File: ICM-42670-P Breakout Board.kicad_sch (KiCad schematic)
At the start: 12 parts, among them J2 Conn_01x09_Pin, U1 ICM-42670-P, U2 MCP1700x-330xxTT

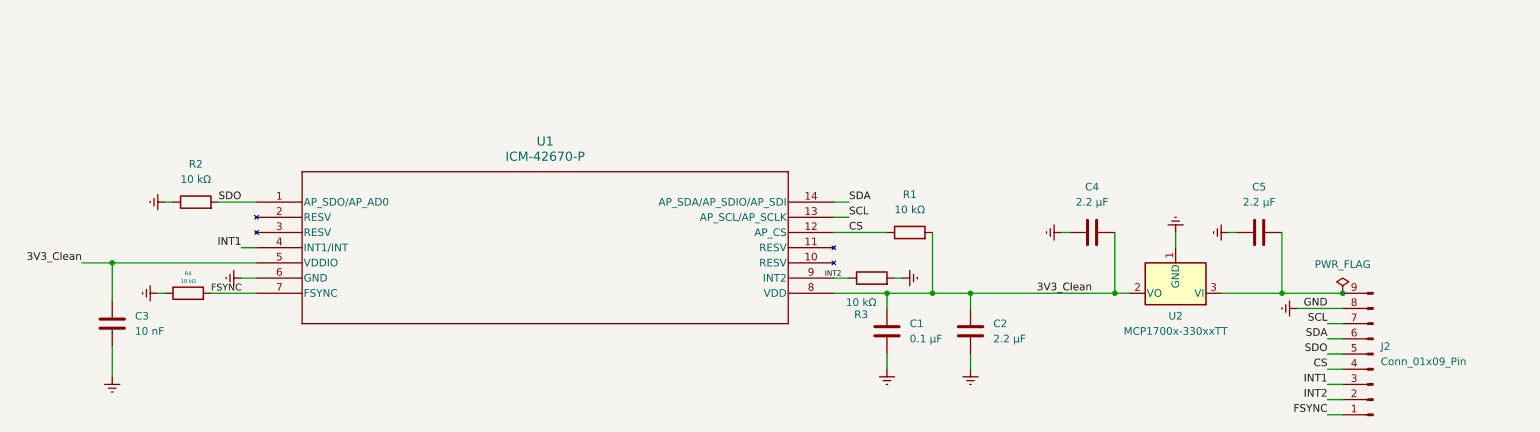
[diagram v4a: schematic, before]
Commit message: Got rid of Resistor on SDO
SDO resister can interfere with SPI and i3C comms, better to let MCU or user Control it
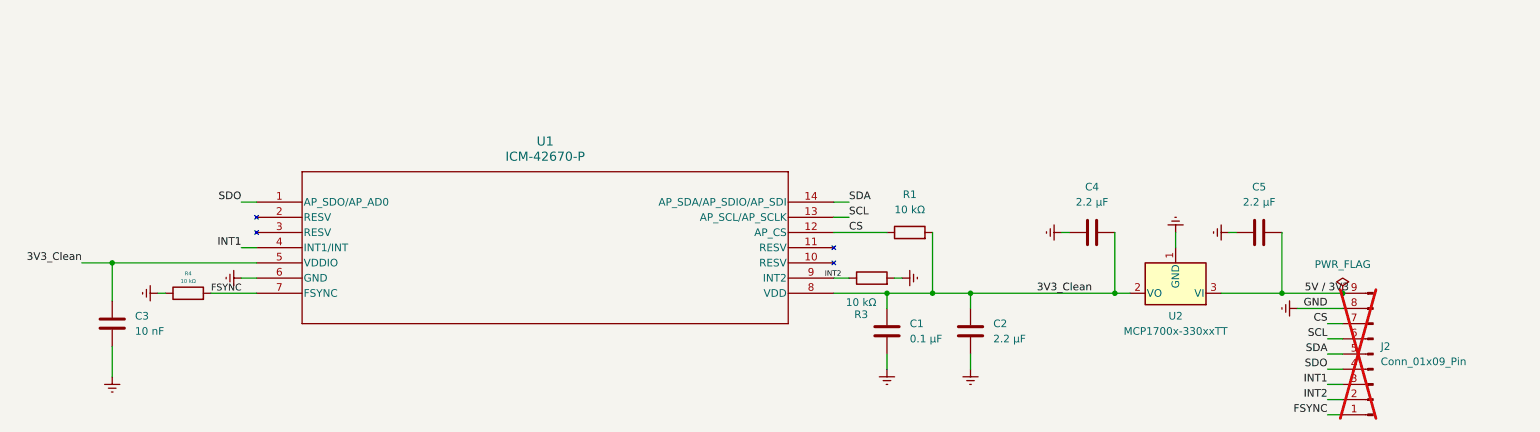
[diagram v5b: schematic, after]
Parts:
- removed R2: 10 kΩ, Resistor_SMD:R_0402_1005Metric, symbol Device:R
- J2: now not fitted
- R1, R3, R4: Specification (none) -> ±1% 0.0625 W (1/16 W)
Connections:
- net CS: now also J2.7 (Pin_7); no longer J2.4 (Pin_4)
- net SCL: now also J2.6 (Pin_6); no longer J2.7 (Pin_7)
- net SDA: now also J2.5 (Pin_5); no longer J2.6 (Pin_6)
- net SDO: now also J2.4 (Pin_4); no longer J2.5 (Pin_5)
- net 5V / 3V3: now reaches C5.2, J2.9 (Pin_9), U2.3 (VI)
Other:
- company: (none) -> Anthony Hua / SleepPandas
- title: (none) -> ICM-42670-P Motion Sensor Breakout with Power Regulation
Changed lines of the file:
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@@
 	(generator_version "9.0")
 	(paper "A4")
+	(title_block
+		(title "ICM-42670-P Motion Sensor Breakout with Power Regulation")
+		(date "2026-MARCH-07")
+		(rev "v1.0")
+		(company "Anthony Hua / SleepPandas")
+	)
 	(junction
 		(at 241.3 101.6)
@@
 	(wire
 		(pts
-			(xy 238.76 111.76) (xy 241.3 111.76)
+			(xy 238.76 106.68) (xy 241.3 106.68)
 		)
 		(stroke
@@
 	(wire
 		(pts
-			(xy 238.76 109.22) (xy 241.3 109.22)
+			(xy 156.21 86.36) (xy 158.75 86.36)
 		)
 		(stroke
@@
 	(wire
 		(pts
-			(xy 156.21 86.36) (xy 158.75 86.36)
+			(xy 57.15 86.36) (xy 59.69 86.36)
 		)
 		(stroke
@@
 	(wire
 		(pts
-			(xy 231.14 101.6) (xy 241.3 101.6)
-		)
-		(stroke
-			(width 0)
-			(type default)
-		)
-	)
-	(wire
-		(pts
-			(xy 238.76 114.3) (xy 241.3 114.3)
+			(xy 233.68 104.14) (xy 241.3 104.14)
 		)
 		(stroke
@@
 	(wire
 		(pts
-			(xy 233.68 104.14) (xy 241.3 104.14)
+			(xy 220.98 101.6) (xy 231.14 101.6)
 		)
 		(stroke
@@
 	(wire
 		(pts
-			(xy 238.76 106.68) (xy 241.3 106.68)
+			(xy 238.76 121.92) (xy 241.3 121.92)
 		)
 		(stroke
@@
 	(wire
 		(pts
-			(xy 220.98 101.6) (xy 231.14 101.6)
+			(xy 222.25 91.44) (xy 223.52 91.44)
 		)
 		(stroke
@@
 	(wire
 		(pts
-			(xy 238.76 121.92) (xy 241.3 121.92)
+			(xy 238.76 119.38) (xy 241.3 119.38)
 		)
 		(stroke
@@
 	(wire
 		(pts
-			(xy 222.25 91.44) (xy 223.52 91.44)
+			(xy 57.15 93.98) (xy 59.69 93.98)
 		)
 		(stroke
@@
 	(wire
 		(pts
-			(xy 238.76 119.38) (xy 241.3 119.38)
+			(xy 238.76 116.84) (xy 241.3 116.84)
 		)
 		(stroke
@@
 	(wire
 		(pts
-			(xy 57.15 93.98) (xy 59.69 93.98)
+			(xy 231.14 91.44) (xy 231.14 101.6)
 		)
 		(stroke
@@
 	(wire
 		(pts
-			(xy 238.76 116.84) (xy 241.3 116.84)
+			(xy 179.07 101.6) (xy 203.2 101.6)
 		)
 		(stroke
@@
 	(wire
 		(pts
-			(xy 231.14 91.44) (xy 231.14 101.6)
+			(xy 35.56 110.49) (xy 35.56 115.57)
 		)
 		(stroke
@@
 	(wire
 		(pts
-			(xy 179.07 101.6) (xy 203.2 101.6)
+			(xy 238.76 109.22) (xy 241.3 109.22)
 		)
 		(stroke
@@
 	(wire
 		(pts
-			(xy 35.56 110.49) (xy 35.56 115.57)
+			(xy 231.14 101.6) (xy 241.3 101.6)
 		)
 		(stroke
@@
 	(wire
 		(pts
-			(xy 53.34 86.36) (xy 59.69 86.36)
+			(xy 165.1 111.76) (xy 165.1 114.3)
 		)
 		(stroke
@@
 	(wire
 		(pts
-			(xy 165.1 111.76) (xy 165.1 114.3)
+			(xy 166.37 99.06) (xy 167.64 99.06)
 		)
 		(stroke
@@
 	(wire
 		(pts
-			(xy 44.45 86.36) (xy 45.72 86.36)
+			(xy 238.76 111.76) (xy 241.3 111.76)
 		)
 		(stroke
@@
 	(wire
 		(pts
-			(xy 166.37 99.06) (xy 167.64 99.06)
+			(xy 172.72 101.6) (xy 179.07 101.6)
 		)
 		(stroke
@@
 	(wire
 		(pts
-			(xy 172.72 101.6) (xy 179.07 101.6)
+			(xy 165.1 101.6) (xy 165.1 104.14)
 		)
 		(stroke
@@
 	(wire
 		(pts
-			(xy 165.1 101.6) (xy 165.1 104.14)
+			(xy 238.76 114.3) (xy 241.3 114.3)
 		)
 		(stroke
@@
 	)
 	(label "CS"
-		(at 238.76 114.3 180)
+		(at 238.76 106.68 180)
 		(effects
 			(font
@@
 		)
 	)
+	(label "5V {slash} 3V3"
+		(at 234.95 101.6 0)
+		(effects
+			(font
+				(size 1.27 1.27)
+			)
+			(justify left bottom)
+		)
+	)
 	(label "SCL"
 		(at 158.75 88.9 0)
@@
 	)
 	(label "SDO"
-		(at 238.76 111.76 180)
+		(at 238.76 114.3 180)
 		(effects
 			(font
@@
 	)
 	(label "SDA"
-		(at 238.76 109.22 180)
+		(at 238.76 111.76 180)
 		(effects
 			(font
@@
 	)
 	(label "SCL"
-		(at 238.76 106.68 180)
+		(at 238.76 109.22 180)
 		(effects
 			(font
@@
 		(in_bom yes)
 		(on_board yes)
-		(dnp no)
+		(dnp yes)
 		(fields_autoplaced yes)
 		(property "Reference" "J2"
@@
 			)
 		)
+		(property "Specification" "±1% 0.0625 W (1/16 W)"
+			(at 168.91 91.44 90)
+			(effects
+				(font
+					(size 1.27 1.27)
+				)
+				(hide yes)
+			)
+		)
 		(pin "2"
 		)
@@
 	(symbol
 		(lib_id "power:Earth")
-		(at 44.45 86.36 270)
-		(unit 1)
-		(exclude_from_sim no)
-		(in_bom yes)
-		(on_board yes)
-		(dnp no)
-		(fields_autoplaced yes)
-		(property "Reference" "#PWR017"
-			(at 38.1 86.36 0)
-			(effects
-				(font
-					(size 1.27 1.27)
-				)
-				(hide yes)
-			)
-		)
-		(property "Value" "GND"
-			(at 40.64 86.3599 90)
-			(effects
-				(font
-					(size 1.27 1.27)
-				)
-				(justify right)
-				(hide yes)
-			)
-		)
-		(property "Footprint" ""
-			(at 44.45 86.36 0)
-			(effects
-				(font
-					(size 1.27 1.27)
-				)
-				(hide yes)
-			)
-		)
-		(property "Datasheet" "~"
-			(at 44.45 86.36 0)
-			(effects
-				(font
-					(size 1.27 1.27)
-				)
-				(hide yes)
-			)
-		)
-		(property "Description" "Power symbol creates a global label with name \"Earth\""
-			(at 44.45 86.36 0)
-			(effects
-				(font
-					(size 1.27 1.27)
-				)
-				(hide yes)
-			)
-		)
-		(pin "1"
-		)
-		(instances
-			(project ""
-				(path "/46f757aa-f0ff-4bf0-8e74-16936fa9d7c2"
-					(reference "#PWR017")
-					(unit 1)
-				)
-			)
-		)
-	)
-	(symbol
-		(lib_id "power:Earth")
 		(at 233.68 104.14 270)
 		(unit 1)
@@
 			)
 		)
+		(property "Specification" "±1% 0.0625 W (1/16 W)"
+			(at 48.26 101.6 90)
+			(effects
+				(font
+					(size 1.27 1.27)
+				)
+				(hide yes)
+			)
+		)
 		(pin "2"
 		)
@@
 	)
 	(symbol
+		(lib_name "C_1")
 		(lib_id "Device:C")
 		(at 227.33 91.44 90)
@@
 			)
 		)
+		(property "Specification" "±1% 0.0625 W (1/16 W)"
+			(at 162.56 99.06 90)
+			(effects
+				(font
+					(size 1.27 1.27)
+				)
+				(hide yes)
+			)
+		)
 		(pin "2"
 		)
@@
 	)
 	(symbol
-		(lib_id "Device:R")
-		(at 49.53 86.36 90)
-		(unit 1)
-		(exclude_from_sim no)
-		(in_bom yes)
-		(on_board yes)
-		(dnp no)
-		(fields_autoplaced yes)
-		(property "Reference" "R2"
-			(at 49.53 80.01 90)
-			(effects
-				(font
-					(size 1.27 1.27)
-				)
-			)
-		)
-		(property "Value" "10 kΩ"
-			(at 49.53 82.55 90)
-			(effects
-				(font
-					(size 1.27 1.27)
-				)
-			)
-		)
-		(property "Footprint" "Resistor_SMD:R_0402_1005Metric"
-			(at 49.53 88.138 90)
-			(effects
-				(font
-					(size 1.27 1.27)
-				)
-				(hide yes)
-			)
-		)
-		(property "Datasheet" "~"
-			(at 49.53 86.36 0)
-			(effects
-				(font
-					(size 1.27 1.27)
-				)
-				(hide yes)
-			)
-		)
-		(property "Description" "Resistor"
-			(at 49.53 86.36 0)
-			(effects
-				(font
-					(size 1.27 1.27)
-				)
-				(hide yes)
-			)
-		)
-		(pin "2"
-		)
-		(pin "1"
-		)
-		(instances
-			(project "ICM-42688-P Breakout Board"
-				(path "/46f757aa-f0ff-4bf0-8e74-16936fa9d7c2"
-					(reference "R2")
-					(unit 1)
-				)
-			)
-		)
-	)
-	(symbol
 		(lib_id "Device:C")
 		(at 179.07 107.95 0)
@@
 	)
 	(embedded_fonts no)
+	(embedded_files
+		(file
+			(name "Draw.kicad_wks")
+			(type worksheet)
+			(data |KLUv/WAECj0VAFbeXyDwWDfQsSwzzQ+NxFWaF2Yhlyyb60htn+WZmgWewXn7VFYATwBaAJ9nEf9j
+				b8QP+tgsZ1/7yZ3YeY+Hhjov2aAHrcmvDQ31mu0pO/qTfwEACAhG0vtIXgyrY1nQO+FodcbfZb/+
+				MSzmnBiVtC+2o+ylAiAgGIlMHbD7rKgQnufJiRUAf7FndqU9wqM1rf6Tv/dVYpW2rKhT/q79zkfP
+				2W/G34ctW1qiD4dee/j220Hf4CXh3LXVf10U8UebNngdgbWcsz93P7KsdrG7H9+JGXs6+9hdMNol
+				u3jKZsAQe42g20bDlByzWFgtmReiGXJWLFsGo206j8yxSVSEetWWczKuRCsWK43LHh1Nk8lsKkI3
+				/LtHzhmV/a9/jfLYH5FClfbMULS2DAGBgSZoZWAUQ1AGNhNUYnRyFY2Cut0oYgeiXlRKeSlo14uh
+				4FSyC8XiUES47MJpWiSzWGAXgpJVtMkGsZDPht3bVlxyahNu48K3HJ10grbfHZQZHFYDcLM6gIKg
+				8USGmJkSUZgkKXSARKTmqBvcLGt61Ov0GmMtRspN6ePryEhYdd4Zdt3vqhHCMWA+Vx2YBFRFjQ10
+				v7/yB/HrlrTSW8DzSTIPOJrFk+BJ19kyUKQVZo7tyclTk53NC8lJt2Oa4/JPE/OpDO4plFCTWdpW
+				DPc5ILzpriyJD7CvDGfUQECbOeXLBMFKWFQQYILlaTRUu5RqmCwbpw7iC/qfTIxJCzlohs/TEzUM
+				aMjpH31l2dzksKfcoq659NJWGwqEdOe0JwoUvHEWH/zmmPdoK2BncUu03EXv/TJsXoNLryAQxOrJ
+				KQFNTR5hDBDkWYfoUzII9kKCyauBA0PHrh4tc7bkSULLcrK2IcRN/Ia9S68mNU3TxvpvLA9Rd5nr
+				QzoGqwo=|
+			)
+			(checksum "EA453518717EB0DF5586ED4C77A0ADB3")
+		)
+	)
 )

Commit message: Got rid of Pull down Resistor for INT2
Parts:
- removed R3: 10 kΩ, Resistor_SMD:R_0402_1005Metric, symbol Device:R
- renumbered R4 to R3
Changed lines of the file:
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@@
 	)
 	(junction
+		(at 53.34 101.6)
+		(diameter 0)
+		(color 0 0 0 0)
+	)
+	(junction
 		(at 231.14 101.6)
 		(diameter 0)
@@
 	(wire
 		(pts
-			(xy 52.07 101.6) (xy 59.69 101.6)
+			(xy 53.34 106.68) (xy 53.34 101.6)
 		)
 		(stroke
@@
 	(wire
 		(pts
-			(xy 166.37 99.06) (xy 167.64 99.06)
+			(xy 238.76 111.76) (xy 241.3 111.76)
 		)
 		(stroke
@@
 	(wire
 		(pts
-			(xy 238.76 111.76) (xy 241.3 111.76)
+			(xy 172.72 101.6) (xy 179.07 101.6)
 		)
 		(stroke
@@
 	(wire
 		(pts
-			(xy 172.72 101.6) (xy 179.07 101.6)
+			(xy 165.1 101.6) (xy 165.1 104.14)
 		)
 		(stroke
@@
 	(wire
 		(pts
-			(xy 165.1 101.6) (xy 165.1 104.14)
+			(xy 238.76 114.3) (xy 241.3 114.3)
 		)
 		(stroke
@@
 	(wire
 		(pts
-			(xy 238.76 114.3) (xy 241.3 114.3)
+			(xy 35.56 96.52) (xy 59.69 96.52)
 		)
 		(stroke
@@
 	(wire
 		(pts
-			(xy 35.56 96.52) (xy 59.69 96.52)
+			(xy 53.34 101.6) (xy 52.07 101.6)
+		)
+		(stroke
+			(width 0)
+			(type default)
+		)
+	)
+	(wire
+		(pts
+			(xy 53.34 101.6) (xy 59.69 101.6)
 		)
 		(stroke
@@
 	)
 	(label "FSYNC"
-		(at 52.07 101.6 0)
+		(at 53.34 106.68 0)
 		(effects
 			(font
@@
 	(symbol
 		(lib_id "power:Earth")
-		(at 167.64 99.06 90)
-		(unit 1)
-		(exclude_from_sim no)
-		(in_bom yes)
-		(on_board yes)
-		(dnp no)
-		(fields_autoplaced yes)
-		(property "Reference" "#PWR014"
-			(at 173.99 99.06 0)
-			(effects
-				(font
-					(size 1.27 1.27)
-				)
-				(hide yes)
-			)
-		)
-		(property "Value" "GND"
-			(at 171.45 99.0599 90)
-			(effects
-				(font
-					(size 1.27 1.27)
-				)
-				(justify right)
-				(hide yes)
-			)
-		)
-		(property "Footprint" ""
-			(at 167.64 99.06 0)
-			(effects
-				(font
-					(size 1.27 1.27)
-				)
-				(hide yes)
-			)
-		)
-		(property "Datasheet" "~"
-			(at 167.64 99.06 0)
-			(effects
-				(font
-					(size 1.27 1.27)
-				)
-				(hide yes)
-			)
-		)
-		(property "Description" "Power symbol creates a global label with name \"Earth\""
-			(at 167.64 99.06 0)
-			(effects
-				(font
-					(size 1.27 1.27)
-				)
-				(hide yes)
-			)
-		)
-		(pin "1"
-		)
-		(instances
-			(project ""
-				(path "/46f757aa-f0ff-4bf0-8e74-16936fa9d7c2"
-					(reference "#PWR014")
-					(unit 1)
-				)
-			)
-		)
-	)
-	(symbol
-		(lib_id "power:Earth")
 		(at 35.56 115.57 0)
 		(unit 1)
@@
 		(on_board yes)
 		(dnp no)
-		(property "Reference" "R4"
+		(property "Reference" "R3"
 			(at 48.26 98.298 90)
 			(effects
@@
 			(project "ICM-42670-P Breakout Board"
 				(path "/46f757aa-f0ff-4bf0-8e74-16936fa9d7c2"
-					(reference "R4")
+					(reference "R3")
 					(unit 1)
 				)
@@
 					(unit 1)
 				)
-			)
-		)
-	)
-	(symbol
-		(lib_id "Device:R")
-		(at 162.56 99.06 90)
-		(unit 1)
-		(exclude_from_sim no)
-		(in_bom yes)
-		(on_board yes)
-		(dnp no)
-		(property "Reference" "R3"
-			(at 160.782 105.156 90)
-			(effects
-				(font
-					(size 1.27 1.27)
-				)
-			)
-		)
-		(property "Value" "10 kΩ"
-			(at 160.782 103.124 90)
-			(effects
-				(font
-					(size 1.27 1.27)
-				)
-			)
-		)
-		(property "Footprint" "Resistor_SMD:R_0402_1005Metric"
-			(at 162.56 100.838 90)
-			(effects
-				(font
-					(size 1.27 1.27)
-				)
-				(hide yes)
-			)
-		)
-		(property "Datasheet" "~"
-			(at 162.56 99.06 0)
-			(effects
-				(font
-					(size 1.27 1.27)
-				)
-				(hide yes)
-			)
-		)
-		(property "Description" "Resistor"
-			(at 162.56 99.06 0)
-			(effects
-				(font
-					(size 1.27 1.27)
-				)
-				(hide yes)
-			)
-		)
-		(property "Specification" "±1% 0.0625 W (1/16 W)"
-			(at 162.56 99.06 90)
-			(effects
-				(font
-					(size 1.27 1.27)
-				)
-				(hide yes)
-			)
-		)
-		(pin "2"
-		)
-		(pin "1"
-		)
-		(instances
-			(project "ICM-42688-P Breakout Board"
-				(path "/46f757aa-f0ff-4bf0-8e74-16936fa9d7c2"
-					(reference "R3")
-					(unit 1)
-				)

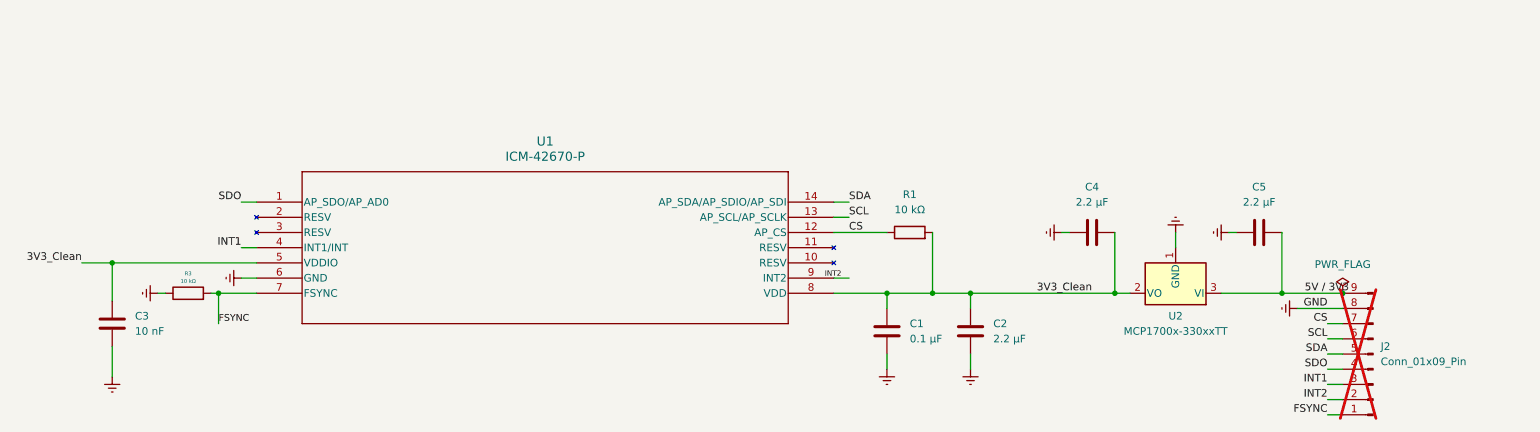
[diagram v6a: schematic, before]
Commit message: Traces Routed
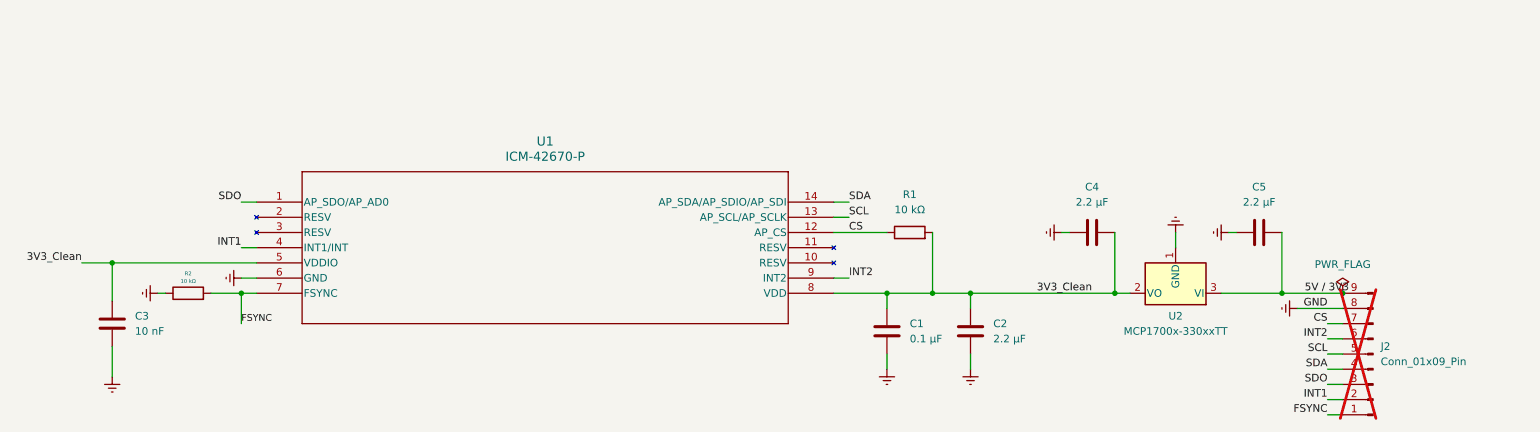
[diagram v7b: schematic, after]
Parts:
- renumbered R3 to R2
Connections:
- net INT1: now also J2.2 (Pin_2); no longer J2.3 (Pin_3)
- net INT2: now also J2.6 (Pin_6); no longer J2.2 (Pin_2)
- net SCL: now also J2.5 (Pin_5); no longer J2.6 (Pin_6)
- net SDA: now also J2.4 (Pin_4); no longer J2.5 (Pin_5)
- net SDO: now also J2.3 (Pin_3); no longer J2.4 (Pin_4)
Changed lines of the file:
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@@
 	)
 	(junction
-		(at 53.34 101.6)
+		(at 231.14 101.6)
 		(diameter 0)
 		(color 0 0 0 0)
 	)
 	(junction
-		(at 231.14 101.6)
+		(at 57.15 101.6)
 		(diameter 0)
 		(color 0 0 0 0)
@@
 	(wire
 		(pts
-			(xy 238.76 106.68) (xy 241.3 106.68)
+			(xy 156.21 86.36) (xy 158.75 86.36)
 		)
 		(stroke
@@
 	(wire
 		(pts
-			(xy 156.21 86.36) (xy 158.75 86.36)
+			(xy 57.15 86.36) (xy 59.69 86.36)
 		)
 		(stroke
@@
 	(wire
 		(pts
-			(xy 57.15 86.36) (xy 59.69 86.36)
+			(xy 156.21 101.6) (xy 165.1 101.6)
 		)
 		(stroke
@@
 	(wire
 		(pts
-			(xy 156.21 101.6) (xy 165.1 101.6)
+			(xy 179.07 101.6) (xy 179.07 104.14)
 		)
 		(stroke
@@
 	(wire
 		(pts
-			(xy 179.07 101.6) (xy 179.07 104.14)
+			(xy 238.76 119.38) (xy 241.3 119.38)
 		)
 		(stroke
@@
 	(wire
 		(pts
-			(xy 233.68 104.14) (xy 241.3 104.14)
+			(xy 238.76 114.3) (xy 241.3 114.3)
 		)
 		(stroke
@@
 	(wire
 		(pts
-			(xy 220.98 101.6) (xy 231.14 101.6)
+			(xy 238.76 106.68) (xy 241.3 106.68)
 		)
 		(stroke
@@
 	(wire
 		(pts
-			(xy 238.76 121.92) (xy 241.3 121.92)
+			(xy 233.68 104.14) (xy 241.3 104.14)
 		)
 		(stroke
@@
 	(wire
 		(pts
-			(xy 222.25 91.44) (xy 223.52 91.44)
+			(xy 220.98 101.6) (xy 231.14 101.6)
 		)
 		(stroke
@@
 	(wire
 		(pts
-			(xy 238.76 119.38) (xy 241.3 119.38)
+			(xy 238.76 121.92) (xy 241.3 121.92)
 		)
 		(stroke
@@
 	(wire
 		(pts
-			(xy 57.15 93.98) (xy 59.69 93.98)
+			(xy 222.25 91.44) (xy 223.52 91.44)
 		)
 		(stroke
@@
 	(wire
 		(pts
-			(xy 231.14 91.44) (xy 231.14 101.6)
+			(xy 57.15 93.98) (xy 59.69 93.98)
 		)
 		(stroke
@@
 	(wire
 		(pts
-			(xy 179.07 101.6) (xy 203.2 101.6)
+			(xy 231.14 91.44) (xy 231.14 101.6)
 		)
 		(stroke
@@
 	(wire
 		(pts
-			(xy 35.56 110.49) (xy 35.56 115.57)
+			(xy 179.07 101.6) (xy 203.2 101.6)
 		)
 		(stroke
@@
 	(wire
 		(pts
-			(xy 238.76 109.22) (xy 241.3 109.22)
+			(xy 35.56 110.49) (xy 35.56 115.57)
 		)
 		(stroke
@@
 	(wire
 		(pts
-			(xy 231.14 101.6) (xy 241.3 101.6)
+			(xy 238.76 111.76) (xy 241.3 111.76)
 		)
 		(stroke
@@
 	(wire
 		(pts
-			(xy 203.2 101.6) (xy 205.74 101.6)
+			(xy 231.14 101.6) (xy 241.3 101.6)
 		)
 		(stroke
@@
 	(wire
 		(pts
-			(xy 165.1 101.6) (xy 172.72 101.6)
+			(xy 203.2 101.6) (xy 205.74 101.6)
 		)
 		(stroke
@@
 	(wire
 		(pts
-			(xy 194.31 91.44) (xy 195.58 91.44)
+			(xy 57.15 101.6) (xy 59.69 101.6)
 		)
 		(stroke
@@
 	(wire
 		(pts
-			(xy 156.21 88.9) (xy 158.75 88.9)
+			(xy 165.1 101.6) (xy 172.72 101.6)
 		)
 		(stroke
@@
 	(wire
 		(pts
-			(xy 179.07 111.76) (xy 179.07 114.3)
+			(xy 194.31 91.44) (xy 195.58 91.44)
 		)
 		(stroke
@@
 	(wire
 		(pts
-			(xy 53.34 106.68) (xy 53.34 101.6)
+			(xy 156.21 88.9) (xy 158.75 88.9)
 		)
 		(stroke
@@
 	(wire
 		(pts
-			(xy 172.72 91.44) (xy 172.72 101.6)
+			(xy 179.07 111.76) (xy 179.07 114.3)
 		)
 		(stroke
@@
 	(wire
 		(pts
-			(xy 165.1 111.76) (xy 165.1 114.3)
+			(xy 57.15 106.68) (xy 57.15 101.6)
 		)
 		(stroke
@@
 	(wire
 		(pts
-			(xy 238.76 111.76) (xy 241.3 111.76)
+			(xy 172.72 91.44) (xy 172.72 101.6)
 		)
 		(stroke
@@
 	(wire
 		(pts
-			(xy 172.72 101.6) (xy 179.07 101.6)
+			(xy 165.1 111.76) (xy 165.1 114.3)
 		)
 		(stroke
@@
 	(wire
 		(pts
-			(xy 165.1 101.6) (xy 165.1 104.14)
+			(xy 172.72 101.6) (xy 179.07 101.6)
 		)
 		(stroke
@@
 	(wire
 		(pts
-			(xy 238.76 114.3) (xy 241.3 114.3)
+			(xy 165.1 101.6) (xy 165.1 104.14)
 		)
 		(stroke
@@
 	(wire
 		(pts
-			(xy 35.56 96.52) (xy 59.69 96.52)
+			(xy 238.76 109.22) (xy 241.3 109.22)
 		)
 		(stroke
@@
 	(wire
 		(pts
-			(xy 53.34 101.6) (xy 52.07 101.6)
+			(xy 35.56 96.52) (xy 59.69 96.52)
 		)
 		(stroke
@@
 	(wire
 		(pts
-			(xy 53.34 101.6) (xy 59.69 101.6)
+			(xy 52.07 101.6) (xy 57.15 101.6)
 		)
 		(stroke
@@
 		)
 	)
-	(label "INT2"
-		(at 157.48 99.06 180)
-		(effects
-			(font
-				(size 0.889 0.889)
-			)
-			(justify right bottom)
-		)
-	)
 	(label "FSYNC"
-		(at 53.34 106.68 0)
+		(at 57.15 106.68 0)
 		(effects
 			(font
@@
 	)
 	(label "INT2"
-		(at 238.76 119.38 180)
+		(at 238.76 109.22 180)
 		(effects
 			(font
@@
 	)
 	(label "SDO"
-		(at 238.76 114.3 180)
+		(at 238.76 116.84 180)
 		(effects
 			(font
@@
 	)
 	(label "SDA"
-		(at 238.76 111.76 180)
+		(at 238.76 114.3 180)
 		(effects
 			(font
@@
 	)
 	(label "SCL"
-		(at 238.76 109.22 180)
+		(at 238.76 111.76 180)
 		(effects
 			(font
@@
 		)
 	)
+	(label "INT2"
+		(at 158.75 99.06 0)
+		(effects
+			(font
+				(size 1.27 1.27)
+			)
+			(justify left bottom)
+		)
+	)
 	(label "INT1"
 		(at 57.15 93.98 180)
@@
 	)
 	(label "INT1"
-		(at 238.76 116.84 180)
+		(at 238.76 119.38 180)
 		(effects
 			(font
@@
 		(on_board yes)
 		(dnp no)
-		(property "Reference" "R3"
+		(property "Reference" "R2"
 			(at 48.26 98.298 90)
 			(effects
@@
 			(project "ICM-42670-P Breakout Board"
 				(path "/46f757aa-f0ff-4bf0-8e74-16936fa9d7c2"
-					(reference "R3")
+					(reference "R2")
 					(unit 1)
 				)
